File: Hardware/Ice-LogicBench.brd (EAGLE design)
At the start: 121 x 100 mm, 114 parts, among them IC1 S27KL0641DABHV020, IC2 S26KL128SDABHI020, IC3 USBLC6-2SC6, IC4 ICE40HX4K-BG121, IC5 FUSB302MPX, IC6 USBLC6-2SC6, J2 QWIIC_RIGHT_ANGLE, Y3 12MZ

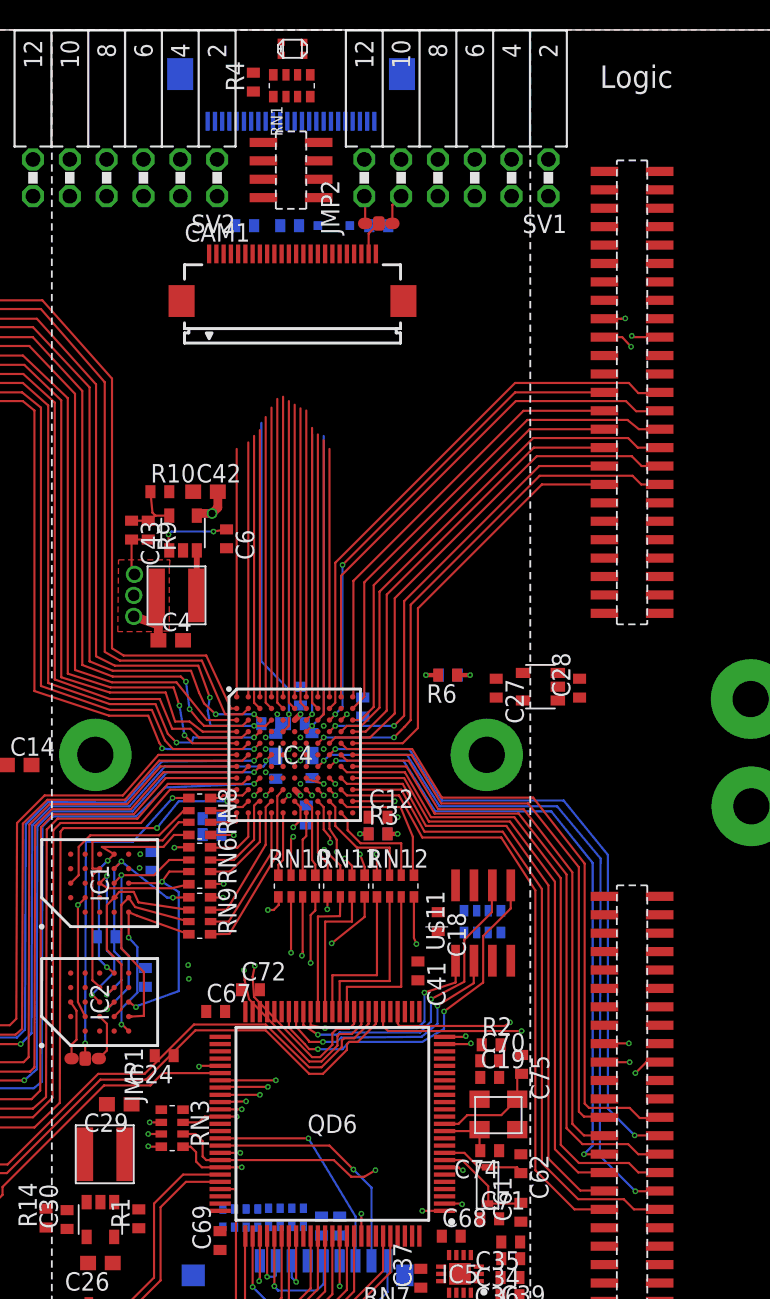
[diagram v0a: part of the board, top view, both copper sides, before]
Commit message: REarranged TG/F pinouts for pait matches updated schematic and previews
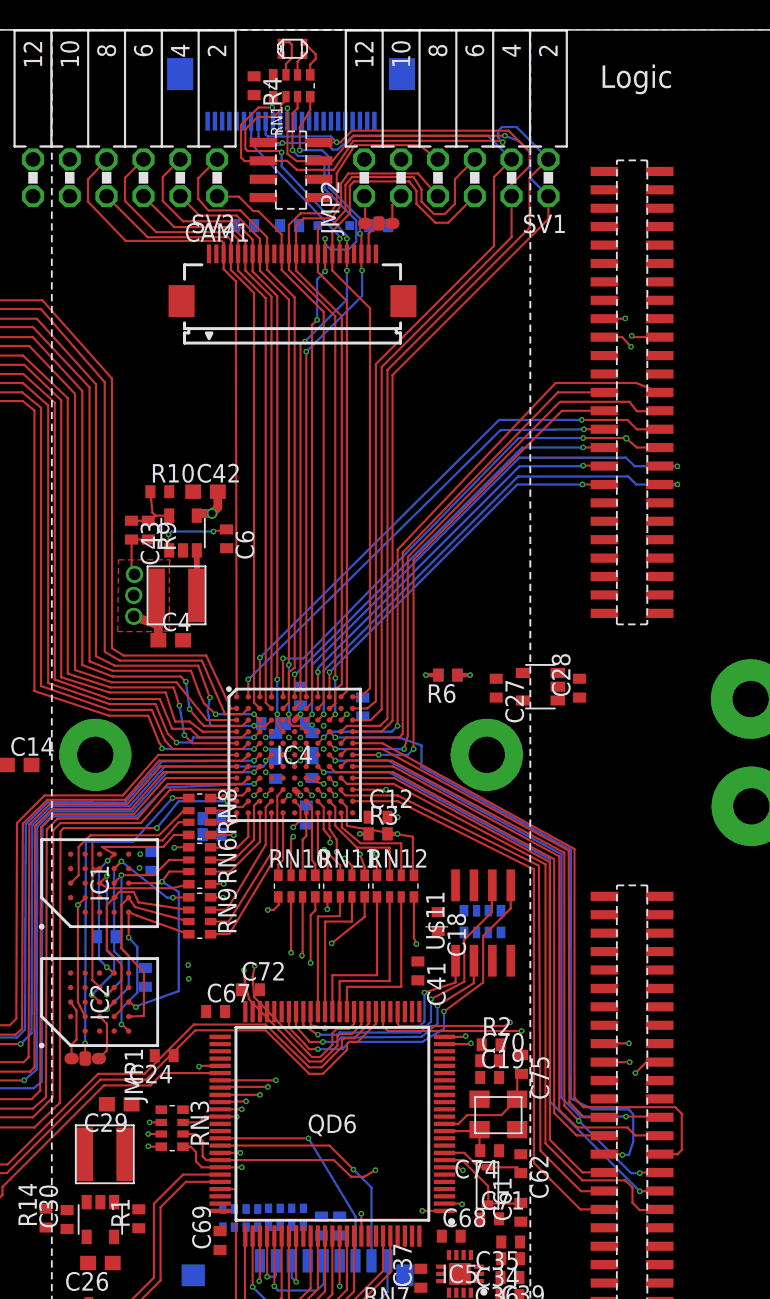
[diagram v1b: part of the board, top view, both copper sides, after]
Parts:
- moved R4 0.25 mm to (58.0, 96.2), turned to 270 degrees
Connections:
- net B/EN: now also RN1.7; no longer RN1.8
- net G/SDA: now also IC4.A7, RN1.8; no longer IC4.A6, RN1.6
- net N$1: now also RN1.1; no longer RN1.3
- net N$3: now also RN1.3; no longer RN1.2
- net N$5: now also RN1.2; no longer RN1.1
- net P1: now also IC4.B3; no longer IC4.A3
- net P10: now also IC4.A10; no longer IC4.C7
- net P11: now also IC4.A11; no longer IC4.A8
- net P12: now also IC4.B11; no longer IC4.D7
- net P13: now also IC4.C11; no longer IC4.C8
- net P14: now also IC4.D10; no longer IC4.A9
- net P15: now also IC4.D11; no longer IC4.B8
- net P2: now also IC4.B4; no longer IC4.A2
- net P3: now also IC4.A4; no longer IC4.B3
- net P4: now also IC4.D5; no longer IC4.B4
- net P5: now also IC4.D7; no longer IC4.D5
- net P6: now also IC4.B5; no longer IC4.A4
- net P7: now also IC4.B8; no longer IC4.B5
- net P8: now also IC4.C9; no longer IC4.A5
- net P9: now also IC4.B9; no longer IC4.A7
- net R/SCL: now also RN1.6; no longer RN1.7
- net RX: now also IC4.J11; no longer IC4.K11
- net TF0: now also IC4.A9; no longer IC4.E11
- net TF1: now also IC4.C8; no longer IC4.E8
- net TF10: now also IC4.E10; no longer IC4.C9
- net TF11: now also IC4.E8; no longer IC4.B9
- net TF2: now also IC4.A8; no longer IC4.D9
- net TF3: now also IC4.C7; no longer IC4.E9
- net TF4: now also IC4.A6; no longer IC4.D11
- net TF5: now also IC4.A5; no longer IC4.D10
- net TF6: now also IC4.A2; no longer IC4.C11
- net TF7: now also IC4.A3; no longer IC4.B11
- net TF8: now also IC4.F11; no longer IC4.A11
- net TF9: now also IC4.E9; no longer IC4.A10
- net TG0: now also IC4.K11; no longer IC4.J10
- net TG1: now also IC4.H10; no longer IC4.J11
- net TG10: now also IC4.F10; no longer IC4.F11
- net TG11: now also IC4.F9; no longer IC4.E10
- net TG2: now also IC4.J10; no longer IC4.H10
- net TG6: now also IC4.D9; no longer IC4.G9
- net TG7: now also IC4.E11; no longer IC4.G11
- net TG8: now also IC4.G9; no longer IC4.F10
- net TG9: now also IC4.G11; no longer IC4.F9
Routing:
- net P14: track 17.1 -> 77.6 mm, vias 0 -> 2
- net P15: track 19.5 -> 69.4 mm, vias 0 -> 2
- net P13: track 19.5 -> 66.6 mm, vias 0 -> 1
- net P12: track 20.9 -> 64.5 mm
- net P10: track 19.9 -> 50.9 mm, vias 1 -> 0
- net P11: track 18.1 -> 48.9 mm
- net P8: track 20.7 -> 50.1 mm, vias 0 -> 2
- net P0: track 17.1 -> 45.6 mm
- net R/SCL: track 21.4 -> 49.7 mm, vias 0 -> 4
- net P9: track 19.8 -> 48.1 mm
- net P2: track 17.5 -> 45.6 mm
- net B/EN: track 20.9 -> 48.7 mm, vias 0 -> 4
- net G/SDA: track 20.2 -> 45.9 mm, vias 0 -> 4
- net P4: track 20.3 -> 45.4 mm, vias 0 -> 2
- net P1: track 18.4 -> 43.0 mm
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
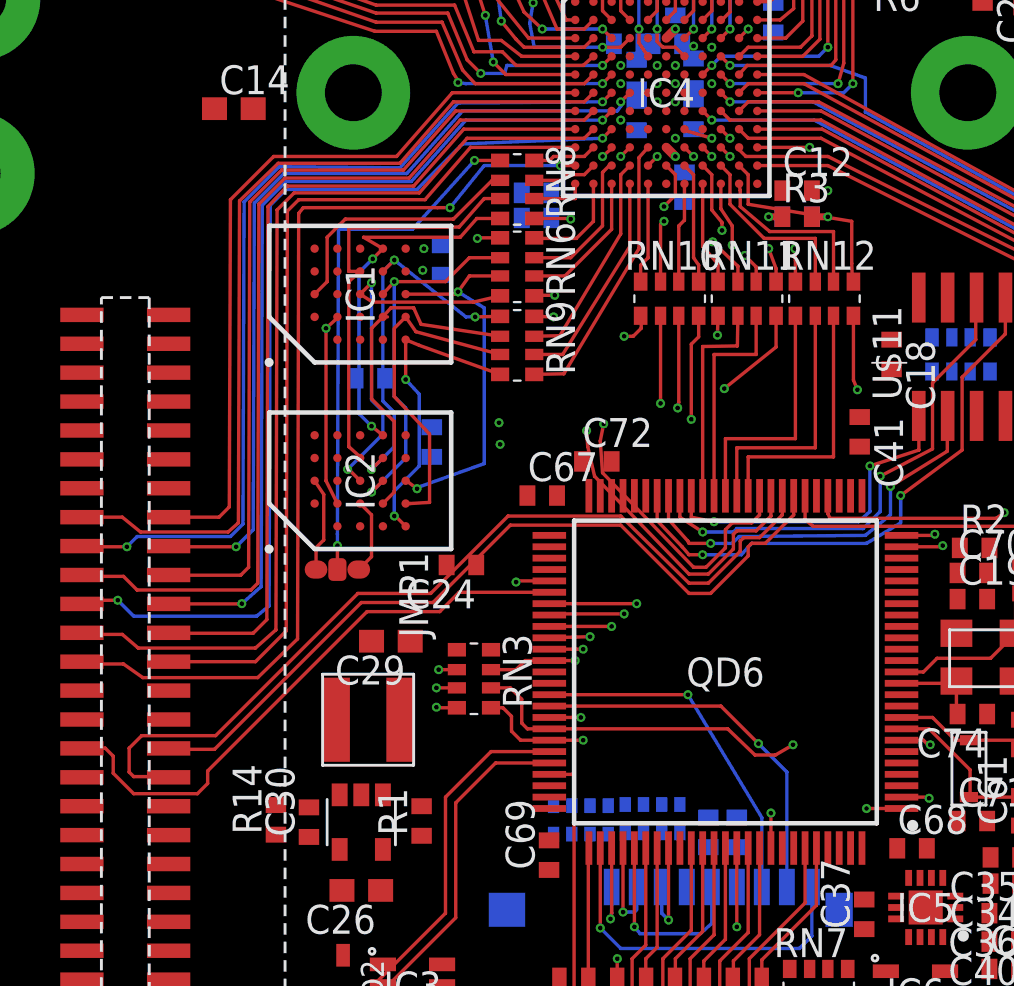
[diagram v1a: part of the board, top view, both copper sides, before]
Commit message: Improved the routing a little
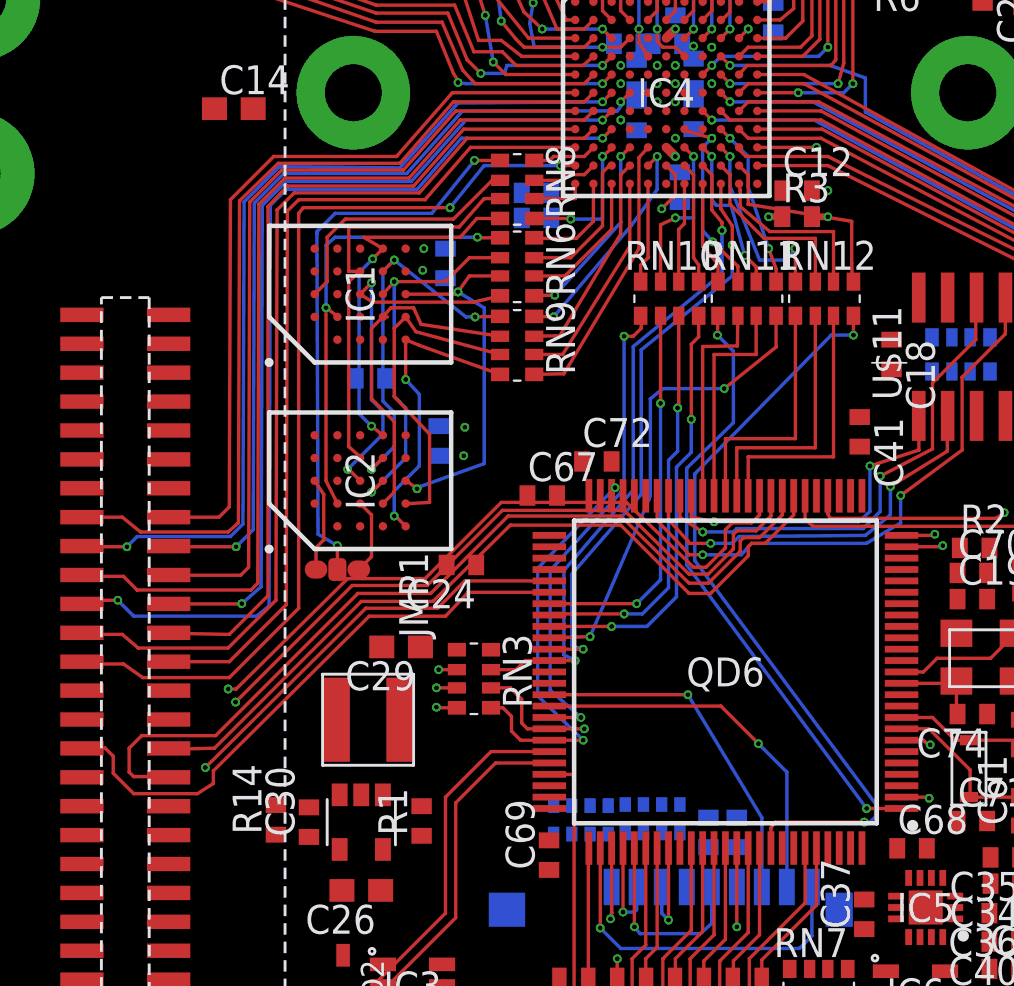
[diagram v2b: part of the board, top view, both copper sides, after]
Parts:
- moved C29 0.51 mm to (49.1, 25.6)
- moved C23 0.30 mm to (50.8, 34.7)
- moved C22 0.21 mm to (51.0, 42.5)
- moved C16 0.20 mm to (61.4, 45.9)
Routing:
- net ADC14: track 64.3 -> 82.9 mm
- net ADC15: track 61.7 -> 79.3 mm
- net TR1: track 55.8 -> 72.1 mm
- net !QSS: track 28.7 -> 33.8 mm
- net QD6: track 24.2 -> 26.9 mm
- net DS0: track 23.4 -> 24.8 mm
- net DQK: track 18.7 -> 20.0 mm
- net TC9: track 43.0 -> 42.3 mm
- net TC11: track 42.2 -> 41.5 mm
- net TC10: track 38.1 -> 37.4 mm
- net RX: track 43.4 -> 42.8 mm
- net QDRX: track 6.70 -> 7.28 mm
- net TC8: track 37.7 -> 37.2 mm
- net TX: vias 2 -> 3

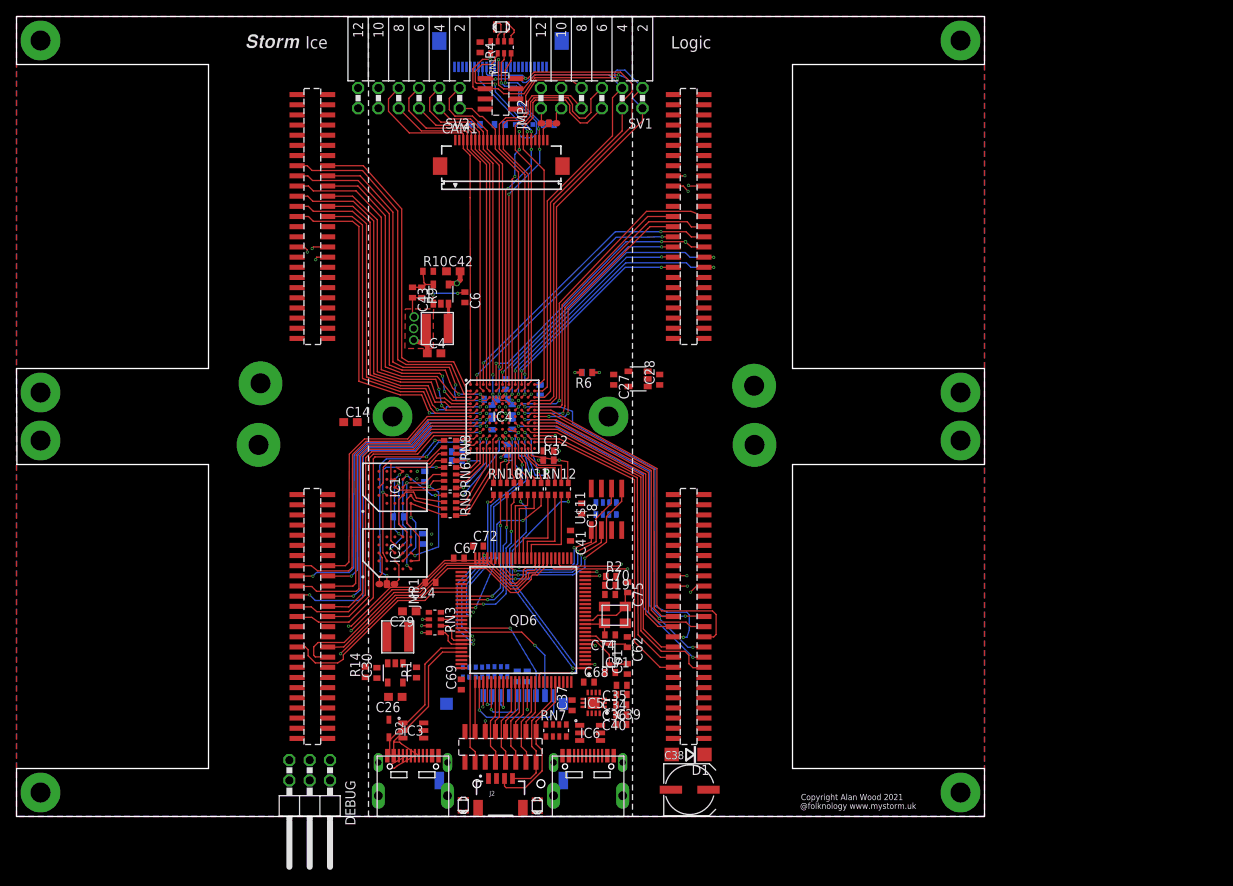
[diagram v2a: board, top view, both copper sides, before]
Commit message: Temporarily added book by disabling the git ignore until I cal work out the continuous Integration required
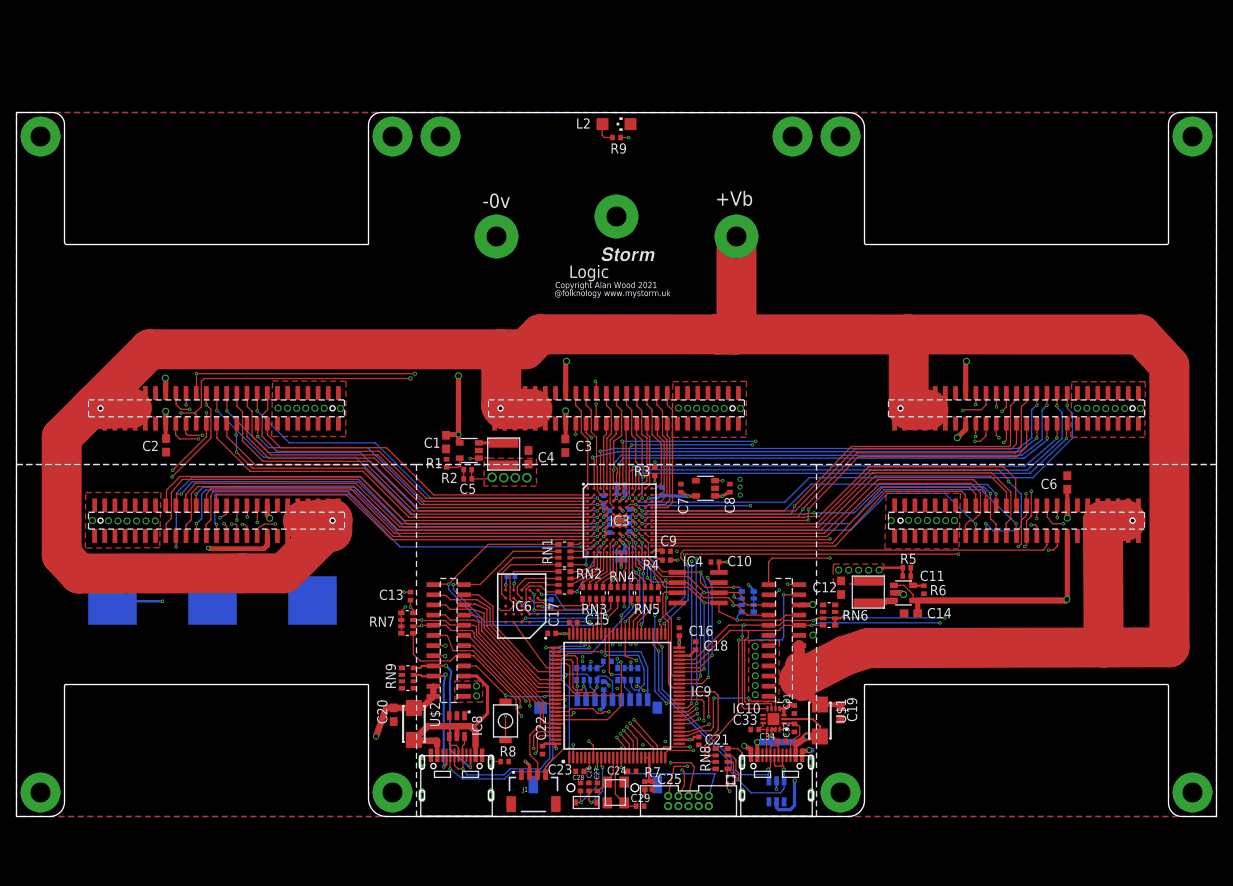
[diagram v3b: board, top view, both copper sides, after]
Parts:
- removed C30, C43, C74, C75: 22pf, rcl:C0402
- removed C35, C40, C41, C67, C68, C69, C70, C72: 470nf, rcl:C0402
- removed C36, C37: 470pf, rcl:C0402
- removed C38: (no value), rcl:UD-6,3X5,8_NICHICON
- removed C39: 6.8nf, rcl:C0402
- removed C42: 22uf, rcl:C0603
- removed C61, C62: 15pf, rcl:C0402
- removed C71: 4u7, rcl:C0402
- removed CAM1, LCD: FH12-24S-0.5SH, con-hirose:FH12-24S-0.5SH
- removed D1: (no value), diode:DO214AC
- removed D2: (no value), zetex:SOD323
- removed D3: (no value), diode:SOD323-R
- removed DEBUG: (no value), pinhead:2X03/90
- removed H2: HOLE2.5MM-LARGE, amino:2M5-LARGE
- removed J2: QWIIC_RIGHT_ANGLE, SparkFun-Connectors:JST04_1MM_RA
- removed JMP1, JMP2: 0R-JUMPC, jump-0r-smd:C0R-JMP
- removed MEZZANINE: HYPER-TILE, amino:HYPER-TILE
- removed QD6: STM32F750V8T6, SamacSys_Parts:QFP50P1600X1600X160-100N
- removed R10: 150k, resistor:R0402
- removed R14: 120k, resistor:R0402
- removed RN10, RN11, RN12: 22r, resistor-dil:EXB38V
- removed SV1, SV2: (no value), con-lsta:FE06-2W
- removed U$10: TF-15X15, amino:SDCARD
- removed U$11: AT25SDF041A, amino:SOIC-8-NARROW
- removed U$12, U$17: RGB_LED0805, amino:RGB-0805
- removed U$13, U$3, U$30, U$31: UTILE_LPCARRIER_SMD_MALE_1.27, amino:UTILE_LP
- removed U$20, U$6: (no value), amino:TSOP-5/SOT23-5
- removed U$23, U$7: NRS4018, amino:NRC4018
- removed U$4: FC-135, amino:FC135
- removed U$8: USB-C-16, amino:USB-C
- removed U$9: NCP114, amino:TSOP-5/SOT23-5
- removed Y3: 12MZ, amino:CRYSTAL-3.2X2.5
- added B1: PUSH_BUTTON, amino:3X4MM_BUTTON
- added BT100: (no value), SparkFun-Batteries:BATTCON_20MM
- added C100, C102, C103, C104, C106, C107, C108, C109, C110, C111, C112: 470nf, rcl:C0402
- added C101, C105, C113: 4u7, rcl:C0402
- added CN1, CN2: USB-C-16, amino:USB-C
- added CN3: 2X5-HEADER, amino:1.27-2X5-HEADER
- added I1, I2: NRS4018, amino:NRC4018
- added IC10: FUSB302MPX, SamacSys_Parts:QFN50P250X250X80-15N
- added IC7, IC8: USBLC6-2SC6, SamacSys_Parts:SOT95P280X145-6N
- added IC9: STM32F750V8T6, SamacSys_Parts:QFP50P1600X1600X160-100N
- added J1: QWIIC_RIGHT_ANGLE, SparkFun-Connectors:JST04_1MM_RA
- added L1: RGB_LED, amino:RGB_LED_IMM
- added L2: (no value), led:CHIPLED_1206
- added R5: 120k, resistor:R0402
- added R7: 100r, resistor:R0402
- added R8: 1k5, resistor:R0402
- added RN100, RN101, RN102: 10k, resistor-dil:EXB38V
- added SD100: TF-15X15, amino:SDCARD
- added TILE1, TILE2, TILE3, TILE4, TILE5: UTILE_LPCARRIER_SMD_MALE_1.27, amino:UTILE_LP
- added TILE6: HYPER-TILECARRIER, amino:HYPER-TILE
- added Y1: 12MZ, amino:CRYSTAL-3.2X2.5
- added Y2: FC-135, amino:FC135
- C1, C12, C2, C20, C3, C6: value 470nf -> 22uf; device rcl:C0402 -> rcl:C0603
- C11, C27, C5: value 470nf -> 22pf
- C13, C15, C31, C34: value 6.8nf -> 470nf
- C19: value 4u7 -> 22uf; device rcl:C0402 -> rcl:C0603
- C21: value 10uf -> 470nf
- C25: value 470nf -> 4u7
- C26: value 22uf -> 15pf; device rcl:C0603 -> rcl:C0402
- C28: value 470nf -> 15pf
- C29: value 22uf -> 22pf; device rcl:C0603 -> rcl:C0402
- C32, C33: value 6.8nf -> 470pf
- IC1: value S27KL0641DABHV020 -> (none); device SamacSys_Parts:BGA24C100P5X5_600X800X100 -> amino:TSOP-5/SOT23-5
- IC2: value S26KL128SDABHI020 -> NCP114; device SamacSys_Parts:BGA24C100P5X5_600X800X100 -> amino:TSOP-5/SOT23-5
- IC3: value USBLC6-2SC6 -> ICE40HX4K-BG121; device SamacSys_Parts:SOT95P280X145-6N -> SamacSys_Parts:BGA121C80P11X11_900X900X110
- IC4: value ICE40HX4K-BG121 -> AT25SDF041A; device SamacSys_Parts:BGA121C80P11X11_900X900X110 -> amino:SOIC-8-NARROW
- IC5: value FUSB302MPX -> (none); device SamacSys_Parts:QFN50P250X250X80-15N -> amino:TSOP-5/SOT23-5
- IC6: value USBLC6-2SC6 -> S27KL0641DABHV020; device SamacSys_Parts:SOT95P280X145-6N -> SamacSys_Parts:BGA24C100P5X5_600X800X100
- R1: value 27k -> 120k
- R2: value 4r -> 120k
- R3, R4: value 100R -> 100r
- R6: value 100R -> 27k
- R9: value 120k -> 1k
- RN1, RN3: value 1k5 -> 22r
- RN2, RN5: value 5k -> 22r; device resistor-dil:0603-ARV -> resistor-dil:EXB38V
- RN4: value 5.1k -> 22r
- RN6, RN9: value 22r -> 5k1
- RN7: value 1k5 -> 5k1
- RN8: value 22r -> 1k5
- U$1: value USB-C-16 -> SS54; device amino:USB-C -> amino:SMA-NARROW
- U$2: value RGB_LED0805 -> SS54; device amino:RGB-0805 -> amino:SMA-NARROW
- moved C32 85.3 mm to (97.2, 11.1), flipped to the top, turned to 90 degrees
- moved C31 81.9 mm to (97.2, 13.4), flipped to the top, turned to 90 degrees
- moved C33 79.9 mm to (92.3, 10.9), flipped to the top, turned to 180 degrees
- moved C6 78.8 mm to (131.3, 41.8)
- moved C14 74.0 mm to (111.8, 25.4)
- moved R4 68.2 mm to (81.2, 32.0), turned to 0 degrees
- moved RN1 63.9 mm to (68.5, 32.8), turned to 270 degrees
- moved C11 55.1 mm to (111.3, 30.1), flipped to the top, turned to 180 degrees
- moved H1 53.1 mm to (75.0, 75.0)
- moved C28 51.9 mm to (70.5, 3.70), turned to 270 degrees
- moved U$1 51.7 mm to (100.4, 12.0), turned to 270 degrees
- moved RN8 51.3 mm to (88.2, 7.22), turned to 90 degrees
- moved C27 50.9 mm to (72.6, 3.70)
- moved RN6 50.4 mm to (101.6, 25.2), turned to 90 degrees
- moved R6 50.1 mm to (113.4, 28.4), turned to 270 degrees
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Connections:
- removed net !CS: QD6.45
- removed net !INT: IC5.5
- removed net ADC2/MISO1: QD6.17
- removed net ADC3/MOSI1: QD6.18
- removed net ADC8/DHS: QD6.28
- removed net B/EN: CAM1.17, IC4.B7, RN1.7
- removed net CC1: C37.1, IC5.10, IC5.11, IC6.6, U$8.CC1
- removed net CC2: C36.2, IC5.1, IC5.14, IC6.4, U$8.CC2
- removed net CRX: MEZZANINE.D1, QD6.51
- removed net CTX: MEZZANINE.D16, QD6.52
- removed net DC2: QD6.97
- removed net DC3: QD6.98
- removed net DC5: QD6.84
- removed net DN: U$8.DN1, U$8.DN2
- removed net DS1: IC1.A3, RN8.2
- removed net DS1X: IC4.K2, RN8.7
- removed net DSF: IC2.C2, JMP1.1
- removed net DSR: IC2.A3, JMP1.3
- removed net DVS: QD6.93
- removed net G/SDA: CAM1.22, IC4.A7, RN1.8
- removed net INT: IC2.A5
- removed net N$15: C23.1, IC2.E4
- removed net N$16: C24.1, IC2.D1
- removed net N$17: C25.1, IC1.D1
- removed net N$20: RN7.1, U$12.B
- removed net N$21: RN7.2, U$12.G
- removed net N$22: RN7.3, U$12.R
- removed net N$23: LCD.1, R4.1
- removed net N$24: RN7.5, U$8.P$1, U$8.P$2, U$8.P$3, U$8.P$4
- removed net N$25: C41.2, QD6.27
- removed net N$26: CAM1.23, JMP2.2
- removed net N$27: IC3.6
- removed net N$28: IC3.4
- removed net N$3: RN1.3, U$17.R
- removed net N$5: RN1.2, U$17.B
- removed net N$7: MEZZANINE.P3
- removed net N$8: RN3.8, U$1.P$1, U$1.P$2, U$1.P$3, U$1.P$4
- removed net N$85: C69.2, QD6.75
- removed net N$86: C67.2, QD6.50
- removed net N$89: C68.2, QD6.100
- removed net N$9: RN2.5, U$1.CC1
- removed net N$90: C71.1, QD6.6
- removed net N$92: C19.1, QD6.20
- removed net QD4: QD6.58, RN10.3
- removed net QD4X: IC4.L7, RN10.6
- removed net QD5: QD6.59, RN10.4
- removed net QD5X: IC4.K7, RN10.5
- removed net QD6: QD6.1, RN11.1
- removed net QD6X: IC4.L8, RN11.8
- removed net QD7: QD6.60, RN11.4
- removed net QD7X: IC4.H9, RN11.5
- removed net QDRX: IC4.J7, RN10.7
- removed net R/SCL: CAM1.20, IC4.B6, RN1.6
- removed net TR10: MEZZANINE.D11, QD6.88
- removed net TR11: MEZZANINE.D7, QD6.90
- removed net TR12: MEZZANINE.D10, QD6.91
- removed net TR7: MEZZANINE.D5, QD6.85
- removed net TR8: MEZZANINE.D12, QD6.86
- removed net TR9: MEZZANINE.D6, QD6.87
- removed net V+: C38.+, D1.C, H2.P$1, H4.P$1, MEZZANINE.V+, U$13.P$20, U$13.P$21, U$13.P$22, U$13.P$23, U$13.P$24, U$13.P$25, U$13.P$45, U$13.P$46, U$13.P$47, U$13.P$48, U$13.P$49, U$13.P$50, U$3.P$20, U$3.P$21, U$3.P$22, U$3.P$23, U$3.P$24, U$3.P$25, U$3.P$45, U$3.P$46, U$3.P$47, U$3.P$48, U$3.P$49, U$3.P$50, U$30.P$20, U$30.P$21, U$30.P$22, U$30.P$23, U$30.P$24, U$30.P$25, U$30.P$45, U$30.P$46, U$30.P$47, U$30.P$48, U$30.P$49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
- removed net V-: C38.-, H1.P$1, H3.P$1, MEZZANINE.V-, U$13.P$1, U$13.P$2, U$13.P$26, U$13.P$27, U$13.P$28, U$13.P$29, U$13.P$3, U$13.P$30, U$13.P$31, U$13.P$4, U$13.P$5, U$13.P$6, U$3.P$1, U$3.P$2, U$3.P$26, U$3.P$27, U$3.P$28, U$3.P$29, U$3.P$3, U$3.P$30, U$3.P$31, U$3.P$4, U$3.P$5, U$3.P$6, U$30.P$1, U$30.P$2, U$30.P$26, U$30.P$27, U$30.P$28, U$30.P$29, U$30.P$3, U$30.P$30, U$30.P$31, U$30.P$4, U$30.P$5, U$30.P$6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
- removed net VBUS: D2.2, IC3.5, IC6.5, U$1.VBUS@1, U$1.VBUS@2
- removed net ~1V8: C31.2, CAM1.15, D3.C
- new net !HRST: IC6.A4, IC9.81
- new net !TRSTA: IC9.97, TILE1.P$15, TILE2.P$15, TILE4.P$15
- new net !TRSTB: IC9.37, TILE3.P$15, TILE5.P$15
- new net ADC2: IC9.17, TILE4.P$42
- new net ADC3: IC9.18, TILE1.P$17
- new net B/!WS: IC3.B7, RN8.6, TILE6.F23
- new net CC1A: CN1.CC1, RN9.7, TILE6.E10
- new net CC1B: C33.1, CN2.CC1, IC10.10, IC10.11
- new net CC2A: CN1.CC2, RN9.8, TILE6.E9
- new net CC2B: C32.2, CN2.CC2, IC10.1, IC10.14
- new net ENA: IC9.98, TILE1.P$40, TILE2.P$40, TILE4.P$40
- new net ENB: IC9.38, TILE3.P$40, TILE5.P$40
- new net G/MT1: IC3.D7, TILE6.F2
- new net GP1: IC9.82, TILE6.E23
- new net GP2: IC9.84, TILE6.E2
- new net GP3: IC9.85, TILE6.E22
- new net GP4: IC9.86, TILE6.E3
- new net GP5: IC9.87, TILE6.E21
- new net GP6: IC9.90, TILE6.E4
- new net GP7: IC9.91, TILE6.E19
- new net GP8: IC9.93, TILE6.E6
- new net HLD: IC4.7, IC9.45
- new net INTU: IC10.5, IC9.28
- new net MODE: IC9.39, RN8.7
- new net MT0: IC3.J11, TILE6.F1
- new net R/!DS: IC3.B6, TILE6.F24
- new net RXX: IC3.J2, RN1.8
- new net SHA: CN1.P$1, CN1.P$2, CN1.P$3, CN1.P$4, R8.1
- new net SHB: CN2.P$1, CN2.P$2, CN2.P$3, CN2.P$4, RN8.4
- new net TXX: IC3.K2, RN1.7
- new net VBAT: BT100.1, C23.1, IC9.6
- new net VBUSA: CN1.VBUS@1, CN1.VBUS@2, IC8.5, TILE6.E15, U$2.A
- new net VBUSB: CN2.VBUS@1, CN2.VBUS@2, IC10.2, U$1.A
- new net WP: IC4.3, IC9.40
- net !QSS: now also IC9.92, RN4.3; no longer QD6.92, RN12.4
- net !QSSX: now also IC3.H9, RN5.5; no longer IC4.K10, RN12.5
- net !SRST: now also C24.2, CN3.6, IC9.14, RN7.5, TILE6.E17; no longer DEBUG.4, MEZZANINE.D3, QD6.14
- net !SS: now also IC3.K10, IC4.1, IC9.41, RN102.4; no longer QD6.41, RN4.2, U$11.1
- net +2V5: now also C112.1, C7.2, IC2.5, IC3.C10; no longer C27.2, C33.2, C5.1, CAM1.21, D3.A, IC4.C10, MEZZANINE.P4, U$9.5
- net +3V3: now also B1.P$1, C100.1, C101.2, C102.1, C103.1, C106.1, C108.1, C11.2, C16.2, C17.2, C2.1, C22.2, C3.2, C31.2, C6.2, C8.2, CN3.1, I2.P$2, IC10.3, IC10.4, IC2.1, IC2.3, IC3.D6, IC3.E4, IC3.F8, IC3.G4, IC3.H6, IC3.L11, IC4.8, IC6.D1, IC6.E4, IC9.100, IC9.27, IC9.50, IC9.75, J1.2, L1.A, R5.2, R7.2, R9.1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; no longer C11.1, C14.2, C18.1, C20.1, C28.2, C29.1, C30.2, C32.2, C34.2, C35.2, C8.1, CAM1.14, DEBUG.6, IC4.D6, IC4.E4, IC4.F8, IC4.G4, IC4.H6, IC4.L11, IC5.3, IC5.4, J2.2, JMP2.1, LCD.4, LCD.5, LCD.6, MEZZANINE.P6, R14.2, R2.2, R4.2, RN1.5, RN2.7, RN2.8, RN4.5, RN4.6, RN4.7, RN4.8, RN5.5, RN5.6, RN5.7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
- net +5V: now also C1.2, C14.2, C20.1, C34.2, H1.P$1, IC1.4, IC10.12, IC10.13, IC5.1, IC5.4, IC7.5, TILE1.P$43, TILE2.P$43, TILE3.P$43, TILE4.P$43, TILE5.P$43, TILE6.E11, TILE6.E12, U$2.C; no longer C26.2, C39.2, C40.2, C42.2, D2.1, IC5.12, IC5.13, U$20.4, U$6.1, U$6.4
- net ADC0: now also IC9.15, TILE4.P$17; no longer QD6.15
- net ADC1: now also IC9.16, TILE4.P$16; no longer QD6.16
- net ADC10/DCCK: now also IC9.30; no longer QD6.30
- net ADC11: now also IC9.31, TILE3.P$17; no longer QD6.31, U$13.P$16
- net ADC12: now also IC9.32, TILE3.P$16; no longer QD6.32, U$31.P$16
- net ADC13: now also IC9.33, TILE3.P$42; no longer QD6.33, U$31.P$17
- net ADC14: now also IC9.34, TILE2.P$17; no longer QD6.34, U$3.P$16
- net ADC15: now also IC9.35, TILE2.P$16; no longer QD6.35, U$3.P$17
- net ADC4: now also IC9.22, TILE1.P$16; no longer QD6.22
- net ADC5: now also IC9.23, TILE1.P$42; no longer QD6.23
- net ADC6: now also IC9.24, TILE5.P$17; no longer QD6.24, U$30.P$17
- net ADC7: now also IC9.25, TILE5.P$16; no longer QD6.25, U$30.P$16
- net ADC9: now also IC9.29, TILE5.P$42; no longer QD6.29, U$13.P$17
- net BOOT: now also B1.P$2, IC9.88, IC9.94, RN100.5, TILE6.E16; no longer QD6.94, RN2.6
- net CLK: now also IC9.67, RN3.4; no longer QD6.67, RN10.1
- net CLKX: now also IC3.L5, RN3.5; no longer IC4.L5, RN10.8
- net D+: now also CN1.DP1, CN1.DP2, IC8.6, IC9.71; no longer IC3.3, QD6.71, U$1.DP1, U$1.DP2
- net D-: now also CN1.DN1, CN1.DN2, IC8.4, IC9.70; no longer IC3.1, QD6.70, U$1.DN1, U$1.DN2
- net DC0: now also IC9.63; no longer QD6.63
- net DC1: now also IC9.64; no longer QD6.64
- net DC4: now also IC9.3; no longer QD6.3
- net DC6: now also IC9.4; no longer QD6.4
- net DC7: now also IC9.5; no longer QD6.5
- net DM: now also CN2.DN1, CN2.DN2, IC7.1, IC9.53; no longer IC6.1, QD6.53
- net DONE: now also IC3.K8, IC9.61, RN8.8; no longer IC4.K8, QD6.62, RN3.7
- net DP: now also CN2.DP1, CN2.DP2, IC7.3, IC9.54; no longer IC6.3, QD6.54, U$8.DP1, U$8.DP2
- net DQ0: now also IC6.D3, RN2.2; no longer IC1.D3, IC2.D3, RN6.2
- net DQ0X: now also IC3.K3, RN2.7; no longer IC4.K3, RN6.7
- net DQ1: now also IC6.D2, RN3.1; no longer IC1.D2, IC2.D2, RN9.2
- net DQ1X: now also IC3.K4, RN3.8; no longer IC4.K4, RN9.7
- net DQ2: now also IC6.C4, RN1.3; no longer IC1.C4, IC2.C4, RN8.3
- net DQ2X: now also IC3.L1, RN1.6; no longer IC4.L1, RN8.6
- net DQ3: now also IC6.D4, RN4.1; no longer IC1.D4, IC2.D4, RN9.1
- net DQ3X: now also IC3.K5, RN4.8; no longer IC4.K5, RN9.8
- net DQ4: now also IC6.D5, RN1.4; no longer IC1.D5, IC2.D5, RN8.4
- net DQ4X: now also IC3.J3, RN1.5; no longer IC4.J3, RN8.5
- net DQ5: now also IC6.E3, RN2.3; no longer IC1.E3, IC2.E3, RN6.3
- net DQ5X: now also IC3.L3, RN2.6; no longer IC4.L3, RN6.6
- net DQ6: now also IC6.E2, RN3.2; no longer IC1.E2, IC2.E2, RN9.3
- net DQ6X: now also IC3.L4, RN3.7; no longer IC4.L4, RN9.6
- net DQ7: now also IC6.E1, RN3.3; no longer IC1.E1, IC2.E1, RN9.4
- net DQ7X: now also IC3.J5, RN3.6; no longer IC4.J5, RN9.5
- net DQK: now also IC6.B2, RN2.1; no longer IC1.B2, IC2.B2, RN6.1
- net DQKX: now also IC3.L2, RN2.8; no longer IC4.L2, RN6.8
- net DQR: now also IC6.C3, RN2.4; no longer IC1.C3, IC2.C3, RN6.4
- net DQRX: now also IC3.J4, RN2.5; no longer IC4.J4, RN6.5
- net DS0: now also IC6.A3, RN4.2; no longer JMP1.2, RN8.1
- net DS0X: now also IC3.K6, RN4.7; no longer IC4.J2, RN8.8
- net GND: now also BT100.2, C100.2, C101.1, C102.2, C103.2, C106.2, C107.1, C108.2, C109.1, C110.1, C112.2, C13.2, C15.2, C16.1, C17.1, C18.1, C19.2, C2.2, C22.1, C23.2, C24.1, C25.2, C29.1, C33.2, C6.1, C8.1, CN1.GND@1, CN1.GND@2, CN2.GND@1, CN2.GND@2, CN3.2, CN3.3, CN3.5, H3.P$1, IC1.2, IC10.8, IC10.9, IC2.2, IC3.E5, IC3.E6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; no longer C11.2, C18.2, C2.1, C29.2, C33.1, C35.1, C36.1, C37.2, C39.1, C40.1, C42.1, C5.2, C6.2, C61.1, C62.1, C70.2, C72.1, C74.1, C75.1, C8.2, CAM1.10, CAM1.24, DEBUG.5, IC3.2, IC4.E5, IC4.E6, IC4.E7, IC4.F5, IC4.F6, IC4.F7, IC4.G5, IC4.G6, IC4.G7, IC4.H5, IC5.8, IC5.9, IC6.2, J2.1, JMP2.3, LCD.2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
- net GPLL0: now also C104.1, C105.1, IC3.L6; no longer C13.1, C16.1, IC4.L6
- net GPLL1: now also C111.1, C113.1, IC3.C5; no longer C15.1, C17.1, IC4.C5
- net N$1: now also L2.A, R9.2; no longer RN1.1, U$17.G
- net N$10: now also C29.2, IC9.13, Y1.3; no longer C75.2, QD6.13, Y3.3
- net N$11: now also C27.2, IC9.12, Y1.1; no longer C74.2, QD6.12, Y3.1
- net N$12: now also C26.2, IC9.9, Y2.P$1; no longer C62.2, QD6.9, U$4.P$1
- net N$13: now also C28.2, IC9.8, Y2.P$2; no longer C61.2, QD6.8, U$4.P$2
- net N$14: now also C15.1, IC9.73; no longer C22.1, IC1.E4
- net N$18: now also C11.1, IC5.5, R5.1, R6.1; no longer C30.1, R1.1, R14.1, U$6.5
- net N$19: now also I2.P$1, IC5.3; no longer U$6.3, U$7.P$1
- net N$2: now also L1.G, RN8.2; no longer RN3.4, U$2.G
- net N$4: now also L1.R, RN8.1; no longer RN3.2, U$2.R
- net N$6: now also L1.B, RN8.3; no longer RN3.3, U$2.B
- net N$87: now also C18.2, IC9.48; no longer C72.2, QD6.48
- net N$88: now also C25.1, IC9.20, IC9.21, R7.1; no longer C70.1, QD6.21, R2.1
- net N$93: now also C5.1, IC1.5, R1.1, R2.1; no longer C43.1, R10.1, R9.1, U$20.5
- net N$94: now also I1.P$1, IC1.3; no longer U$20.3, U$23.P$1
- net P0: now also IC3.A1, TILE2.P$42; no longer CAM1.3, IC4.A1, SV2.8
- net P1: now also IC3.B3, TILE2.P$41; no longer CAM1.4, IC4.B3, SV2.7
- net P10: now also IC3.A10, TILE2.P$10; no longer CAM1.16, IC4.A10, SV1.6
- net P11: now also IC3.A11, TILE2.P$35; no longer CAM1.18, IC4.A11, SV1.5
- net P12: now also IC3.B11, TILE2.P$9; no longer IC4.B11, LCD.8, MEZZANINE.P1, SV1.4
- net P13: now also IC3.C11, TILE2.P$34; no longer IC4.C11, LCD.9, MEZZANINE.P8, SV1.3
- net P14: now also IC3.D10, TILE2.P$8; no longer IC4.D10, LCD.10, MEZZANINE.P2, SV1.2
- net P15: now also IC3.D11, TILE2.P$33; no longer IC4.D11, LCD.12, MEZZANINE.P7, SV1.1
- net P2: now also IC3.B4, TILE2.P$14; no longer CAM1.5, IC4.B4, SV2.6
- net P3: now also IC3.A4, TILE2.P$39; no longer CAM1.6, IC4.A4, SV2.5
- net P4: now also IC3.D5, TILE2.P$13; no longer CAM1.7, IC4.D5, SV2.4
- net P5: now also IC3.B5, TILE2.P$38; no longer CAM1.8, IC4.D7, SV2.3
- net P6: now also IC3.A7, TILE2.P$12; no longer CAM1.9, IC4.B5, SV2.2
- net P7: now also IC3.B8, TILE2.P$37; no longer CAM1.11, IC4.B8, SV2.1
- net P8: now also IC3.C9, TILE2.P$11; no longer CAM1.12, IC4.C9, SV1.8
- net P9: now also IC3.B9, TILE2.P$36; no longer CAM1.13, IC4.B9, SV1.7
- net PEN: now also C13.1, IC1.1, RN7.8; no longer C6.1, RN1.4, U$20.1
- net PRT: now also IC3.L9, IC9.57; no longer CAM1.19, IC1.A4, IC2.A4, IC4.L9, LCD.7, QD6.61
- net QCK: now also IC9.36, RN5.4; no longer QD6.36, RN12.3
- net QCKX: now also IC3.L8, RN5.8; no longer IC4.L10, RN12.6
- net QD0: now also IC9.58, RN5.3; no longer QD6.37, RN12.2
- net QD0X: now also IC3.H7, RN5.7; no longer IC4.K9, RN12.7
- net QD1: now also IC9.59, RN5.2; no longer QD6.38, RN12.1
- net QD1X: now also IC3.K7, RN4.5; no longer IC4.J9, RN12.8
- net QD2: now also IC9.1, RN4.4; no longer QD6.39, RN11.3
- net QD2X: now also IC3.J8, RN5.6; no longer IC4.J8, RN11.6
- net QD3: now also IC9.60, RN5.1; no longer QD6.40, RN11.2
- net QD3X: now also IC3.L7, RN4.6; no longer IC4.H7, RN11.7
- net QDR: now also IC3.J7, IC9.62; no longer QD6.57, RN10.2
- net RX: now also IC9.68, RN1.1, TILE6.E1; no longer IC4.J11, QD6.68, RN3.6
- net SCD: now also IC9.83, RN101.2, SD100.P$7; no longer QD6.83, RN5.2, RN7.8, U$10.P$7
- net SCK: now also IC3.L10, IC4.6, IC9.42, RN102.3, TILE6.F3; no longer QD6.42, RN4.3, U$11.6
- net SCL: now also IC10.6, IC9.46, RN6.8, TILE3.P$39, TILE5.P$39, TILE6.F20; no longer QD6.46
- net SCL2: now also IC9.95, J1.4, RN7.7, TILE1.P$39, TILE4.P$39, TILE6.E20; no longer IC5.6, J2.4, MEZZANINE.D8, QD6.95
- net SD: now also IC9.77, RN100.1, SD100.P$1; no longer QD6.77, RN7.6, U$10.P$1
- net SD0: now also IC9.65, RN100.3, SD100.P$3; no longer QD6.65, RN5.1, U$10.P$3
- net SD1: now also IC9.66, RN100.2, SD100.P$2; no longer QD6.66, RN2.2, U$10.P$2
- net SD2: now also IC9.78, RN101.4, SD100.P$9; no longer QD6.78, RN5.4, U$10.P$9
- net SD3: now also IC9.79, RN101.3, SD100.P$8; no longer QD6.79, RN5.3, U$10.P$8
- net SDA: now also IC10.7, IC9.47, RN6.7, TILE3.P$14, TILE5.P$14, TILE6.F5; no longer QD6.47
- net SDA2: now also IC9.96, J1.3, RN7.6, TILE1.P$14, TILE4.P$14, TILE6.E5; no longer IC5.7, J2.3, MEZZANINE.D9, QD6.96
- net SDK: now also IC9.80, RN101.1, SD100.P$5; no longer QD6.80, RN2.1, U$10.P$5
- net SI: now also IC3.K9, IC4.5, IC9.44, RN102.1, TILE6.F21; no longer QD6.44, RN4.4, U$11.5
- net SO: now also IC3.J9, IC4.2, IC9.43, RN102.2, TILE6.F4; no longer QD6.43, RN4.1, U$11.2
- net SWCLK: now also CN3.9, IC9.76, TILE6.E8; no longer DEBUG.1, MEZZANINE.D15, QD6.76, U$1.SBU2
- net SWDIO: now also CN3.10, IC9.72, TILE6.E7; no longer DEBUG.3, MEZZANINE.D2, QD6.72, U$1.SBU1
- net SWO: now also CN3.8, IC9.89, TILE6.E18; no longer DEBUG.2, MEZZANINE.D14, QD6.89, U$1.CC2
- net TB0: now also IC3.B1, TILE1.P$8; no longer IC4.B1, U$3.P$8
- net TB1: now also IC3.B2, TILE1.P$33; no longer IC4.B2, U$3.P$33
- net TB10: now also IC3.E2, TILE1.P$13; no longer IC4.E2, U$3.P$13
- net TB11: now also IC3.E3, TILE1.P$38; no longer IC4.E3, U$3.P$38
- net TB2: now also IC3.C4, TILE1.P$9; no longer IC4.C4, U$3.P$9
- net TB3: now also IC3.C3, TILE1.P$34; no longer IC4.C3, U$3.P$34
- net TB4: now also IC3.C2, TILE1.P$10; no longer IC4.C2, U$3.P$10
- net TB5: now also IC3.C1, TILE1.P$35; no longer IC4.C1, U$3.P$35
- net TB6: now also IC3.E1, TILE1.P$11; no longer IC4.E1, U$3.P$11
- net TB7: now also IC3.D1, TILE1.P$36; no longer IC4.D1, U$3.P$36
- net TB8: now also IC3.D2, TILE1.P$12; no longer IC4.D2, U$3.P$12
- net TB9: now also IC3.D3, TILE1.P$37; no longer IC4.D3, U$3.P$37
- net TC0: now also IC3.F1, TILE4.P$8; no longer IC4.F1, U$31.P$8
- net TC1: now also IC3.F2, TILE4.P$33; no longer IC4.F2, U$31.P$33
- net TC10: now also IC3.J1, TILE4.P$13; no longer IC4.J1, U$31.P$13
- net TC11: now also IC3.K1, TILE4.P$38; no longer IC4.K1, U$31.P$38
- net TC2: now also IC3.F4, TILE4.P$9; no longer IC4.F4, U$31.P$9
- net TC3: now also IC3.F3, TILE4.P$34; no longer IC4.F3, U$31.P$34
- net TC4: now also IC3.G1, TILE4.P$10; no longer IC4.G1, U$31.P$10
- net TC5: now also IC3.G2, TILE4.P$35; no longer IC4.G2, U$31.P$35
- net TC6: now also IC3.G3, TILE4.P$11; no longer IC4.G3, U$31.P$11
- net TC7: now also IC3.H3, TILE4.P$36; no longer IC4.H3, U$31.P$36
- net TC8: now also IC3.H1, TILE4.P$12; no longer IC4.H1, U$31.P$12
- net TC9: now also IC3.H2, TILE4.P$37; no longer IC4.H2, U$31.P$37
- net TF0: now also IC3.A9, TILE3.P$8; no longer IC4.A9, U$30.P$8
- net TF1: now also IC3.C8, TILE3.P$33; no longer IC4.C8, U$30.P$33
- net TF10: now also IC3.E10, TILE3.P$13; no longer IC4.E10, U$30.P$13
- net TF11: now also IC3.E8, TILE3.P$38; no longer IC4.E8, U$30.P$38
- net TF2: now also IC3.A8, TILE3.P$9; no longer IC4.A8, U$30.P$9
- net TF3: now also IC3.C7, TILE3.P$34; no longer IC4.C7, U$30.P$34
- net TF4: now also IC3.A6, TILE3.P$10; no longer IC4.A6, U$30.P$10
- net TF5: now also IC3.A5, TILE3.P$35; no longer IC4.A5, U$30.P$35
- net TF6: now also IC3.A2, TILE3.P$11; no longer IC4.A2, U$30.P$11
- net TF7: now also IC3.A3, TILE3.P$36; no longer IC4.A3, U$30.P$36
- net TF8: now also IC3.F11, TILE3.P$12; no longer IC4.F11, U$30.P$12
- net TF9: now also IC3.E9, TILE3.P$37; no longer IC4.E9, U$30.P$37
- net TG0: now also IC3.K11, TILE5.P$8; no longer IC4.K11, U$13.P$8
- net TG1: now also IC3.H10, TILE5.P$33; no longer IC4.H10, U$13.P$33
- net TG10: now also IC3.F10, TILE5.P$13; no longer IC4.F10, U$13.P$13
- net TG11: now also IC3.F9, TILE5.P$38; no longer IC4.F9, U$13.P$38
- net TG2: now also IC3.J10, TILE5.P$9; no longer IC4.J10, U$13.P$9
- net TG3: now also IC3.G8, TILE5.P$34; no longer IC4.G8, U$13.P$34
- net TG4: now also IC3.H11, TILE5.P$10; no longer IC4.H11, U$13.P$10
- net TG5: now also IC3.G10, TILE5.P$35; no longer IC4.G10, U$13.P$35
- net TG6: now also IC3.D9, TILE5.P$11; no longer IC4.D9, U$13.P$11
- net TG7: now also IC3.E11, TILE5.P$36; no longer IC4.E11, U$13.P$36
- net TG8: now also IC3.G9, TILE5.P$12; no longer IC4.G9, U$13.P$12
- net TG9: now also IC3.G11, TILE5.P$37; no longer IC4.G11, U$13.P$37
- net TR1: now also IC9.52, TILE3.P$41; no longer QD6.55, U$3.P$41
- net TR2: now also IC9.51, TILE5.P$41; no longer QD6.56, U$31.P$41
- net TR3: now also IC9.2, TILE4.P$41; no longer QD6.2, U$13.P$41
- net TR4: now also IC9.7, TILE1.P$41; no longer QD6.7, U$30.P$41
- net TR5: now also IC9.55; no longer MEZZANINE.D4, QD6.81
- net TR6: now also IC9.56; no longer MEZZANINE.D13, QD6.82
- net TX: now also IC9.69, RN1.2, TILE6.E24; no longer IC4.K6, QD6.69, RN3.5
- net VB+: now also C19.1, H4.P$1, TILE1.P$20, TILE1.P$21, TILE1.P$22, TILE1.P$23, TILE1.P$24, TILE1.P$25, TILE1.P$45, TILE1.P$46, TILE1.P$47, TILE1.P$48, TILE1.P$49, TILE1.P$50, TILE2.P$20, TILE2.P$21, TILE2.P$22, TILE2.P$23, TILE2.P$24, TILE2.P$25, TILE2.P$45, TILE2.P$46, TILE2.P$47, TILE2.P$48, TILE2.P$49, TILE2.P$50, TILE3.P$20, TILE3.P$21, TILE3.P$22, TILE3.P$23, TILE3.P$24, TILE3.P$25, TILE3.P$45, TILE3.P$46, TILE3.P$47, TILE3.P$48, TILE3.P$49, TILE3.P$50, TILE4.P$20, TILE4.P$21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; no longer D1.A, IC5.2, U$8.VBUS@1, U$8.VBUS@2
- net VCC: now also C107.2, C109.2, C110.2, C5.2, I1.P$2, IC3.D4, IC3.D8, IC3.H4, IC3.H8, R2.2, R3.1, R4.2; no longer C1.2, C2.2, C3.2, C43.2, C7.2, IC4.D4, IC4.D8, IC4.H4, IC4.H8, R3.2, R6.1, R9.2, U$23.P$2
- net VPLL0: now also C104.2, C105.2, IC3.J6, R4.1; no longer C13.2, C16.2, IC4.J6, R3.1
- net VPLL1: now also C111.2, C113.2, IC3.C6, R3.2; no longer C15.2, C17.2, IC4.C6, R6.2
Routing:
- net VB+: track 0.00 -> 509.1 mm
- net +5V: track 9.23 -> 384.1 mm, vias 1 -> 10
- net ENA: track 0.00 -> 135.0 mm, vias 0 -> 5
- net !TRSTA: track 0.00 -> 134.8 mm, vias 0 -> 5
- net SCL: track 0.00 -> 85.1 mm, vias 0 -> 5
- net +3V3: track 1.91 -> 85.2 mm, vias 7 -> 39
- net ADC5: track 0.00 -> 81.7 mm, vias 0 -> 2
- net SDA: track 0.00 -> 80.1 mm, vias 0 -> 7
- net ENB: track 0.00 -> 80.1 mm, vias 0 -> 3
- net SCL2: track 16.3 -> 95.8 mm, vias 0 -> 4
- net ADC3: track 0.00 -> 77.6 mm, vias 0 -> 2
- net ADC4: track 0.00 -> 77.6 mm, vias 0 -> 2
- net !TRSTB: track 0.00 -> 77.2 mm, vias 0 -> 3
- net VBAT: track 0.00 -> 74.3 mm, vias 0 -> 2
- net B/!WS: track 0.00 -> 71.5 mm, vias 0 -> 4
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- added copper zone on layer 1, net +3V3
- added copper zone on layer 15, net +3V3
- added copper zone on layer 2, net VCC
- removed copper zone on layer 2, net +3V3
- removed copper zone on layer 15, net VCC
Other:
- board size 121 x 100 mm -> 150 x 88 mm
- board text added: "+Vb"
- board text added: "-0v"
- board text removed: "Hardware for passionate bit wranglers"
- board text removed: "Ice"
- board text removed: "Redo messed up 0402 pad sizes"
